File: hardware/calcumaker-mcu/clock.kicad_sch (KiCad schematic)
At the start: 3 parts, among them Y1 32.768kHz

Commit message: hardware: 3-board split (MCU + keyboard + display), wired display, real connectors
Split the single logic board into three, wire the display as a KiCad
multi-channel design, and settle every interconnect on real, in-stock parts.

Three-board split (was two):
- Rename calcumaker-main -> calcumaker-mcu (brain/PSU logic board).
- New calcumaker-keyboard board: 50-key Cherry MX matrix + its own
  STM32G031K8U6 scanner (LCSC C432207, UFQFPN-32) + annunciator LEDs,
  mezzanine-stacked above the MCU board. Keyscanning is off the main board;
  only an I2C + UART link + KB_IRQ wake + power cross the mezzanine.

Display board (calcumaker-display):
- Corrected FJ5161AH to a SINGLE-digit 0.56" common-cathode part (C8093) --
  it is NOT a 4-digit module; 48 single digits (16/row x 3), authored symbol
  + 0.56" LTS6760 land. The old 4-digit CC56-12 mapping (and its 3D model)
  was the phantom "clock colon".
- Rebuilt as a KiCad multi-channel design: one reusable display_row.kicad_sch
  (1 TM1640 + 16 digits, fully wired) instantiated x3. Extended kschgen.py
  with wiring primitives + reused-sheet (multi-channel) support.

Connectors (real, verified LCSC / DigiKey parts):
- Display link -> 0.5mm 12P FFC: AFC01-S12FCA-00 (LCSC C262661) on both
  boards; cable = GCT FFC05-TIN 05-12-A-<len>-A-4-06-4-T (DigiKey accessory,
  length TBD). +5V/GND conductors doubled for the display LED current.
- Keyboard mezzanine -> low-profile Hirose DF40 (0.4mm, 2x5, 1.5mm stack):
  DF40C-10DS (C424636) + DF40C-10DP (C424635) -- dedicated KiCad footprint
  + 3D model, unlike the datasheet-less generic parts first considered.

Low-power & wake documented (two Stop domains; keypress -> G0 EXTI wake ->
KB_IRQ -> U575 WKUP; G0 also wakes on I2C address-match). calcumaker-core
is unchanged -- App still consumes (row,col).

All three boards generate + pass the structure check (mcu 52 / keyboard 119 /
display 60 components, all footprints assigned, no duplicate refs). Docs
(DESIGN.md, PARTS.md incl. a Non-B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
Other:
- title: Calcumaker 16 — Main — LSE 32.768 kHz (RTC) -> Calcumaker 16 — MCU — LSE 32.768 kHz (RTC)
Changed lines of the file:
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@@
 	(paper "A3")
 	(title_block
-		(title "Calcumaker 16 — Main — LSE 32.768 kHz (RTC)")
-		(date "2026-06-21")
-		(rev "0.1")
+		(title "Calcumaker 16 — MCU — LSE 32.768 kHz (RTC)")
+		(date "2026-07-05")
+		(rev "0.2")
 		(company "calcumaker authors")
 	)
@@
 		(pin "2")
 		(instances
-			(project "calcumaker-main"
-				(path "/ca1c0000-0000-4000-8000-00000000ma01/4dd16969-fa48-40a9-bf37-e7180cf6be85"
+			(project "calcumaker-mcu"
+				(path "/ca1c0000-0000-4000-8000-00000000ma01/dc502c7f-271d-4dc5-a1c2-d18857eddfee"
 					(reference "Y1")
 					(unit 1)
@@
 		(pin "2")
 		(instances
-			(project "calcumaker-main"
-				(path "/ca1c0000-0000-4000-8000-00000000ma01/4dd16969-fa48-40a9-bf37-e7180cf6be85"
+			(project "calcumaker-mcu"
+				(path "/ca1c0000-0000-4000-8000-00000000ma01/dc502c7f-271d-4dc5-a1c2-d18857eddfee"
 					(reference "C24")
 					(unit 1)
@@
 		(pin "2")
 		(instances
-			(project "calcumaker-main"
-				(path "/ca1c0000-0000-4000-8000-00000000ma01/4dd16969-fa48-40a9-bf37-e7180cf6be85"
+			(project "calcumaker-mcu"
+				(path "/ca1c0000-0000-4000-8000-00000000ma01/dc502c7f-271d-4dc5-a1c2-d18857eddfee"
 					(reference "C25")
 					(unit 1)

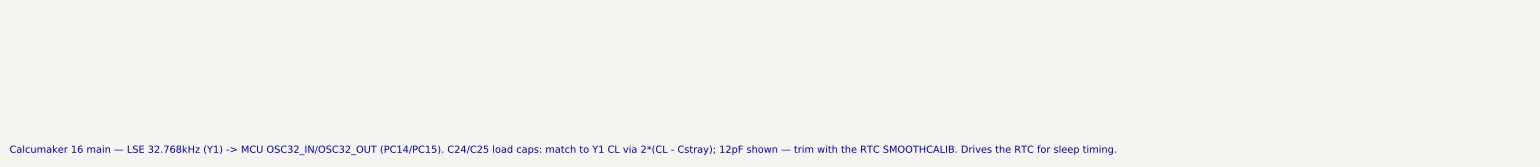
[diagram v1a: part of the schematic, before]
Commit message: docs: accuracy cleanup across README/DESIGN/PARTS + firmware/schgen comments
Sweep the docs and code comments to the three-board reality. Reviewed for
accuracy against the schematics/parts — no factual fixes were needed; this
also corrected several stale spots left over from the split:

- README / DESIGN.md / PARTS.md / reference: three-board split, 0.5mm FFC
  display link, Hirose DF40 mezzanine, STM32G0 keyboard scanner; drop stale
  "main board" phrasing; populate reference/README.md's datasheet table with
  the real parts (STM32G031K8U6, TM1640, FJ5161AH, AFC01-S12FCA-00 + GCT FFC,
  DF40C-10DS/DP).
- DESIGN.md Annunciators corrected to the keyboard board (D51-55 / R1-5,
  driven by the keyboard G0); Open Questions renumbered sequentially.
- firmware comments (keypad.rs / main.rs / Cargo.toml / README): keyboard-event
  intake over the mezzanine link + wake on KB_IRQ; fixed the wrong "host-tested
  with rug" note (it is the gmp-mpfr-nostd FFI). Comment-only, no logic change.
- schgen + .kicad_sch notes: "main" -> "MCU board", FFC/mezzanine references,
  TPS61022/MCU "no custom symbol".

All three boards still pass the structure check (mcu 52 / keyboard 119 /
display 60 components, no duplicate refs); the generator still compiles.

Co-Authored-By: Claude Opus 4.8 (1M context) <noreply@anthropic.com>
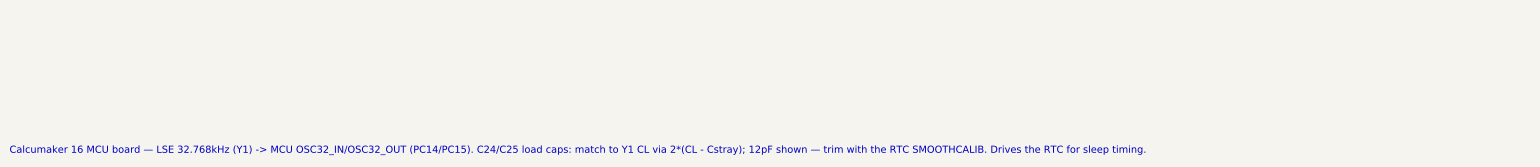
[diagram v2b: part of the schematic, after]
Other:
- note added: "Calcumaker 16 MCU board — LSE 32.768kHz (Y1) -> MCU OSC32_IN/OSC32_OUT (PC14/PC15). C24/C25 load caps: match to Y1 CL via 2*(CL - Cstray); 12pF shown — trim with the RTC SMOOTHCALIB. Drives the RTC for sleep timing."
- note removed: "Calcumaker 16 main — LSE 32.768kHz (Y1) -> MCU OSC32_IN/OSC32_OUT (PC14/PC15). C24/C25 load caps: match to Y1 CL via 2*(CL - Cstray); 12pF shown — trim with the RTC SMOOTHCALIB. Drives the RTC for sleep timing."
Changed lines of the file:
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@@
 		)
 	)
-	(text "Calcumaker 16 main — LSE 32.768kHz (Y1) -> MCU OSC32_IN/OSC32_OUT (PC14/PC15). C24/C25 load caps: match to Y1 CL via 2*(CL - Cstray); 12pF shown — trim with the RTC SMOOTHCALIB. Drives the RTC for sleep timing."
+	(text "Calcumaker 16 MCU board — LSE 32.768kHz (Y1) -> MCU OSC32_IN/OSC32_OUT (PC14/PC15). C24/C25 load caps: match to Y1 CL via 2*(CL - Cstray); 12pF shown — trim with the RTC SMOOTHCALIB. Drives the RTC for sleep timing."
 		(exclude_from_sim no)
 		(at 15.00 100.00 0)

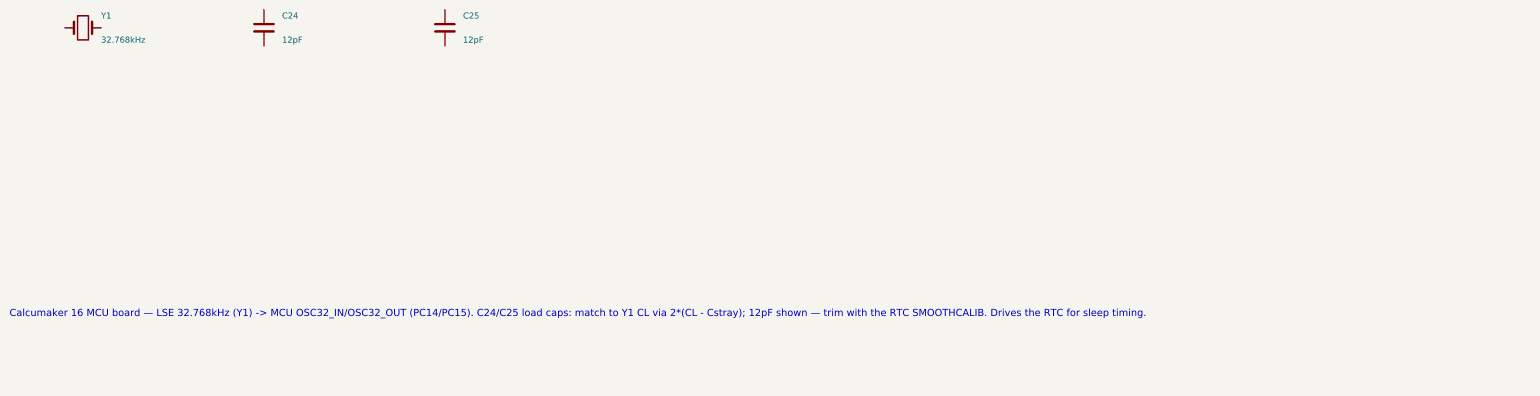
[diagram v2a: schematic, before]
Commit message: hardware: MCU -> STM32U575RGT6 (LQFP-64) + 4MB QSPI flash; monospace wiring notes
MCU package + external flash
- Swap U1 STM32U575ZGT6 (LQFP-144) -> STM32U575RGT6 (LQFP-64, LCSC C5270980).
  The firmware links at ~323 KB so 1 MB flash is ample (~3x headroom), and with
  the key matrix scanned off-board the LQFP-64 has enough GPIO — smaller/cheaper.
- Correct the flash size everywhere: the STM32 `G` code = 1 MB (not 2 MB; the
  `I` parts are 2 MB). memory.x FLASH 2048K -> 1024K; .cargo runner -> RGTx.
- Add U7 W25Q32JVSSIQ, a 4 MB (32 Mbit) quad-SPI NOR (LCSC C179173, SOIC-8) on
  OCTOSPI1 as a new QSPIFlash sheet (+ R9 CS# pull-up + C26 decoupling) for
  memory-mapped (XIP) constants + state/program storage.
- mcu board 52 -> 55 components / 7 sheets. Docs (DESIGN.md, PARTS.md, READMEs,
  CLAUDE/AGENTS) updated; availability ladder now lists RGT6/VGT6/ZGT6.

Monospace, multi-line schematic wiring notes
- kschgen text_note() now renders notes in a monospace font (Courier New) so
  tables/columns line up; add note_block() + pin_table() helpers.
- Reformat all 14 per-sheet notes into titled, multi-line, aligned blocks —
  connector pinouts as PIN/SIGNAL tables, power/MCU sheets as wiring blocks.

The regenerated schematics carry both changes, so this is one commit. All three
boards regenerate + pass the structure check (mcu 55 / keyboard 119 / display
60, no duplicate refs).

Co-Authored-By: Claude Opus 4.8 (1M context) <noreply@anthropic.com>
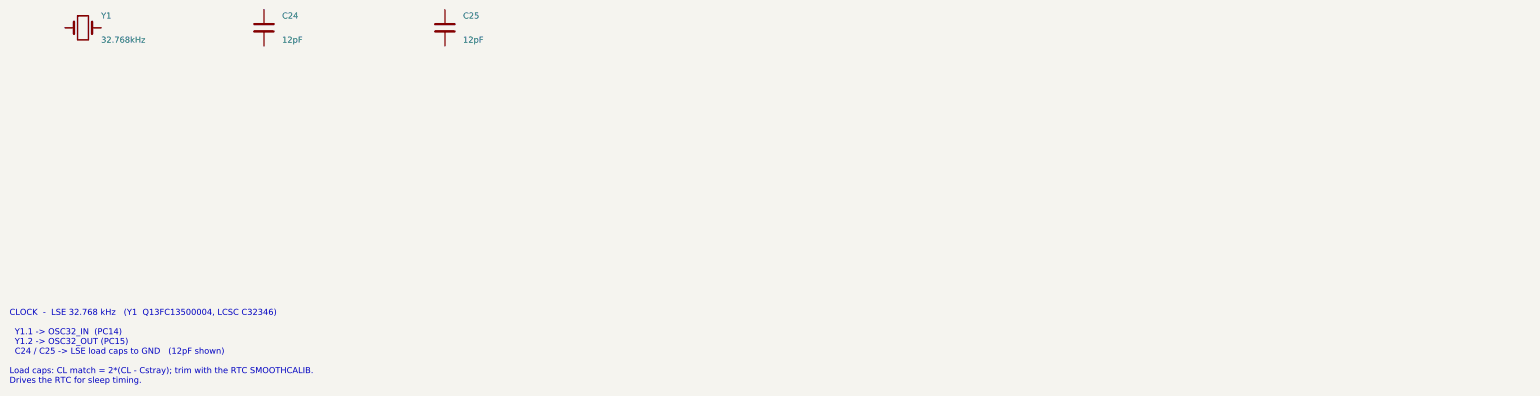
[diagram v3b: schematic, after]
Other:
- note added: "CLOCK - LSE 32.768 kHz (Y1 Q13FC13500004, LCSC C32346) Y1.1 -> OSC32_IN (PC14) Y1.2 -> OSC32_OUT (PC15) C24 / C25 -> LSE load caps to GND (12pF shown) Load caps: CL match = 2*(CL - Cstray); trim with the RTC SMOOTHCALIB. Drives the RTC for sleep timing."
- note removed: "Calcumaker 16 MCU board — LSE 32.768kHz (Y1) -> MCU OSC32_IN/OSC32_OUT (PC14/PC15). C24/C25 load caps: match to Y1 CL via 2*(CL - Cstray); 12pF shown — trim with the RTC SMOOTHCALIB. Drives the RTC for sleep timing."
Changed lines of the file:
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@@
 	(title_block
 		(title "Calcumaker 16 — MCU — LSE 32.768 kHz (RTC)")
-		(date "2026-07-05")
-		(rev "0.2")
+		(date "2026-07-06")
+		(rev "0.3")
 		(company "calcumaker authors")
 	)
@@
 		(instances
 			(project "calcumaker-mcu"
-				(path "/ca1c0000-0000-4000-8000-00000000ma01/dc502c7f-271d-4dc5-a1c2-d18857eddfee"
+				(path "/ca1c0000-0000-4000-8000-00000000ma01/b734f1a0-165b-4dbe-8a4e-b7ae065fd64e"
 					(reference "Y1")
 					(unit 1)
@@
 		(instances
 			(project "calcumaker-mcu"
-				(path "/ca1c0000-0000-4000-8000-00000000ma01/dc502c7f-271d-4dc5-a1c2-d18857eddfee"
+				(path "/ca1c0000-0000-4000-8000-00000000ma01/b734f1a0-165b-4dbe-8a4e-b7ae065fd64e"
 					(reference "C24")
 					(unit 1)
@@
 		(instances
 			(project "calcumaker-mcu"
-				(path "/ca1c0000-0000-4000-8000-00000000ma01/dc502c7f-271d-4dc5-a1c2-d18857eddfee"
+				(path "/ca1c0000-0000-4000-8000-00000000ma01/b734f1a0-165b-4dbe-8a4e-b7ae065fd64e"
 					(reference "C25")
 					(unit 1)
@@
 		)
 	)
-	(text "Calcumaker 16 MCU board — LSE 32.768kHz (Y1) -> MCU OSC32_IN/OSC32_OUT (PC14/PC15). C24/C25 load caps: match to Y1 CL via 2*(CL - Cstray); 12pF shown — trim with the RTC SMOOTHCALIB. Drives the RTC for sleep timing."
+	(text "CLOCK  -  LSE 32.768 kHz   (Y1  Q13FC13500004, LCSC C32346)\n\n  Y1.1 -> OSC32_IN  (PC14)\n  Y1.2 -> OSC32_OUT (PC15)\n  C24 / C25 -> LSE load caps to GND   (12pF shown)\n\nLoad caps: CL match = 2*(CL - Cstray); trim with the RTC SMOOTHCALIB.\nDrives the RTC for sleep timing."
 		(exclude_from_sim no)
 		(at 15.00 100.00 0)
-		(effects (font (size 1.5 1.5)) (justify left top))
+		(effects (font (face "Courier New") (size 1.27 1.27)) (justify left top))
 	)
 	(sheet_instances

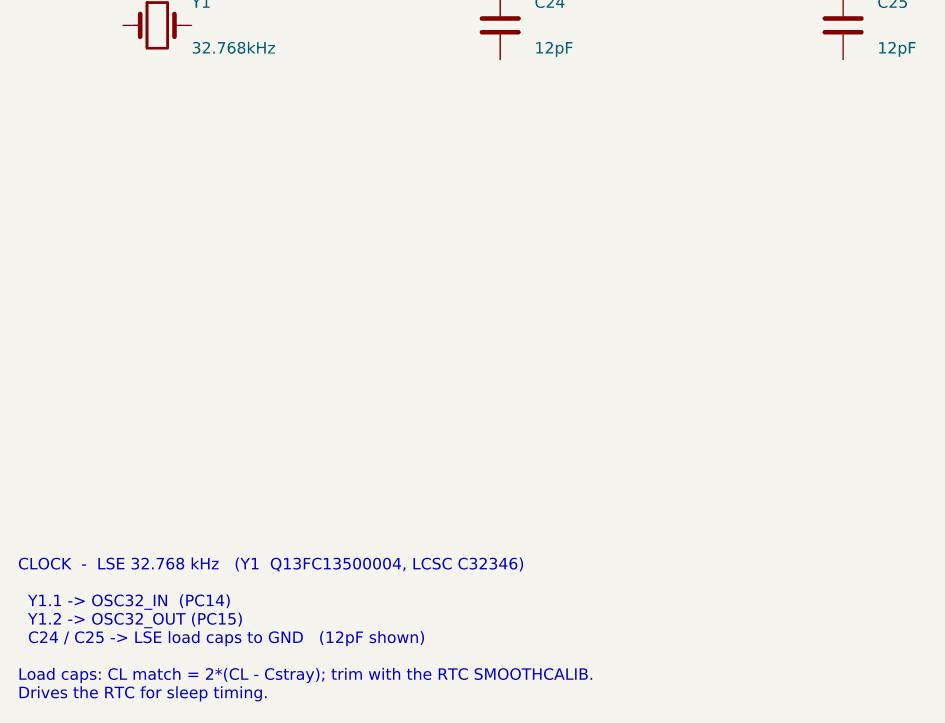
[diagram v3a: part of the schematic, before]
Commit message: hardware: per-key RGB hint lighting on the keyboard board (50x SK6805 on gated VSYS) (#4)
Add addressable RGB accent lighting that hints key positions / presses -- one
SK6805-EC15 (1.5x1.5mm, the smallest serial RGB with a KiCad footprint + real
LCSC stock, C2890035) beside each of the 50 keys, single-wire daisy chain off
one STM32G0 pin.

Power: the LEDs are ~5V parts and the keyboard rail is only 3.3V, so they run
off VSYS (the MCU board's load-shared battery/USB rail, ~3.7-4.7V) brought up a
WIDENED 12-pin mezzanine (10 -> 12: +VSYS +GND). A high-side P-FET load switch
(Q1 AO3401A + Q2 2N7002) gates the whole LED rail off in sleep (G0 LED_EN) to
protect battery life, and a 74LVC1G125 (powered from the gated rail) level-shifts
the 3.3V data up to the LED VIH.

- calcumaker-keyboard: new KeyLighting sheet (50x SK6805 D56-D105 + U2 shifter +
  Q1/Q2 load switch + R7-R10 / C6-C7); J1 mezzanine -> 12-pin DF40C-12DP
  (C6224952). 119 -> 178 components.
- calcumaker-mcu: J5 mezzanine -> 12-pin DF40B-12DS (C3641147); route VSYS.
- DF40 stack: the receptacle SUFFIX sets the mated height (none = 1.5mm,
  (2.0) = 2.0mm, H-series = 2.5-4.0mm), NOT the B/C letter; the DF40C plug is the
  common header -- so DF40C-12DP x DF40B-12DS is a valid 1.5mm stack, same as the
  original 10-pin (DF40C-12DS just isn't LCSC-stocked).
- DESIGN.md / PARTS.md / memory: RGB subsystem, 12-pin pinout, BOM rows, the
  sleep-gate + current-cap notes (firmware must cap total brightness; 50x
  full-white ~0.75A would exceed the DF40 / VSYS budget).

All three boards regenerate + pass the structure check (mcu 55 / keyboard 178 /
display 60, no duplicate refs).

Co-authored-by: Claude Opus 4.8 (1M context) <noreply@anthropic.com>
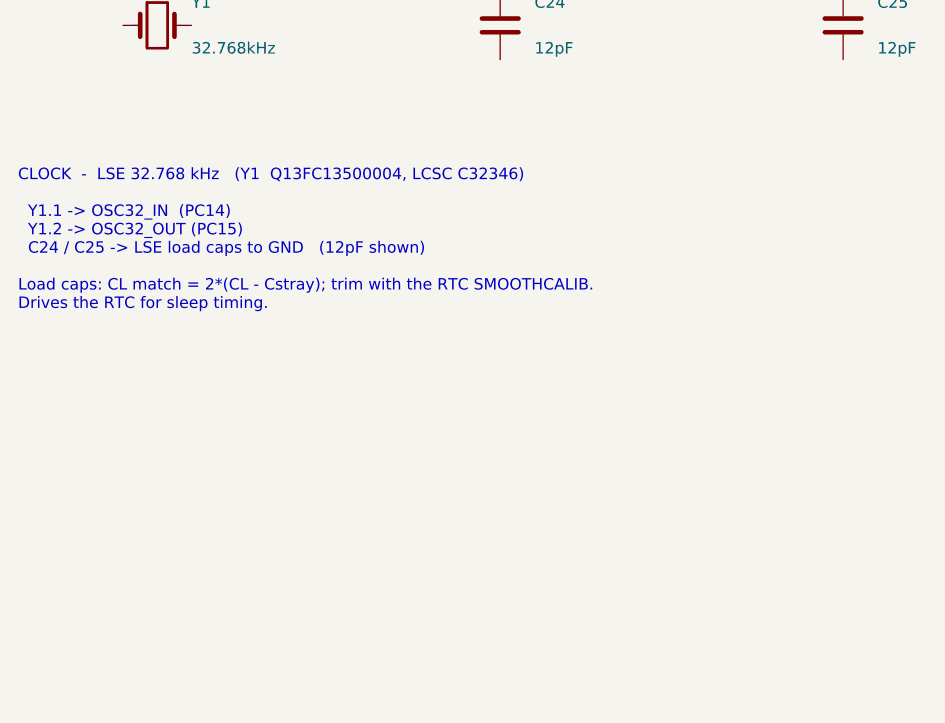
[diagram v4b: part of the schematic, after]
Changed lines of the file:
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@@
 	(text "CLOCK  -  LSE 32.768 kHz   (Y1  Q13FC13500004, LCSC C32346)\n\n  Y1.1 -> OSC32_IN  (PC14)\n  Y1.2 -> OSC32_OUT (PC15)\n  C24 / C25 -> LSE load caps to GND   (12pF shown)\n\nLoad caps: CL match = 2*(CL - Cstray); trim with the RTC SMOOTHCALIB.\nDrives the RTC for sleep timing."
 		(exclude_from_sim no)
-		(at 15.00 100.00 0)
+		(at 15.00 56.64 0)
 		(effects (font (face "Courier New") (size 1.27 1.27)) (justify left top))
 	)
